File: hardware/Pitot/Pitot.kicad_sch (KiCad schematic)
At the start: 35 parts, among them J1 53307-2471, J3 MX150_02x06_Vertical, J4 Conn_01x07, U2 LDO40LPURY

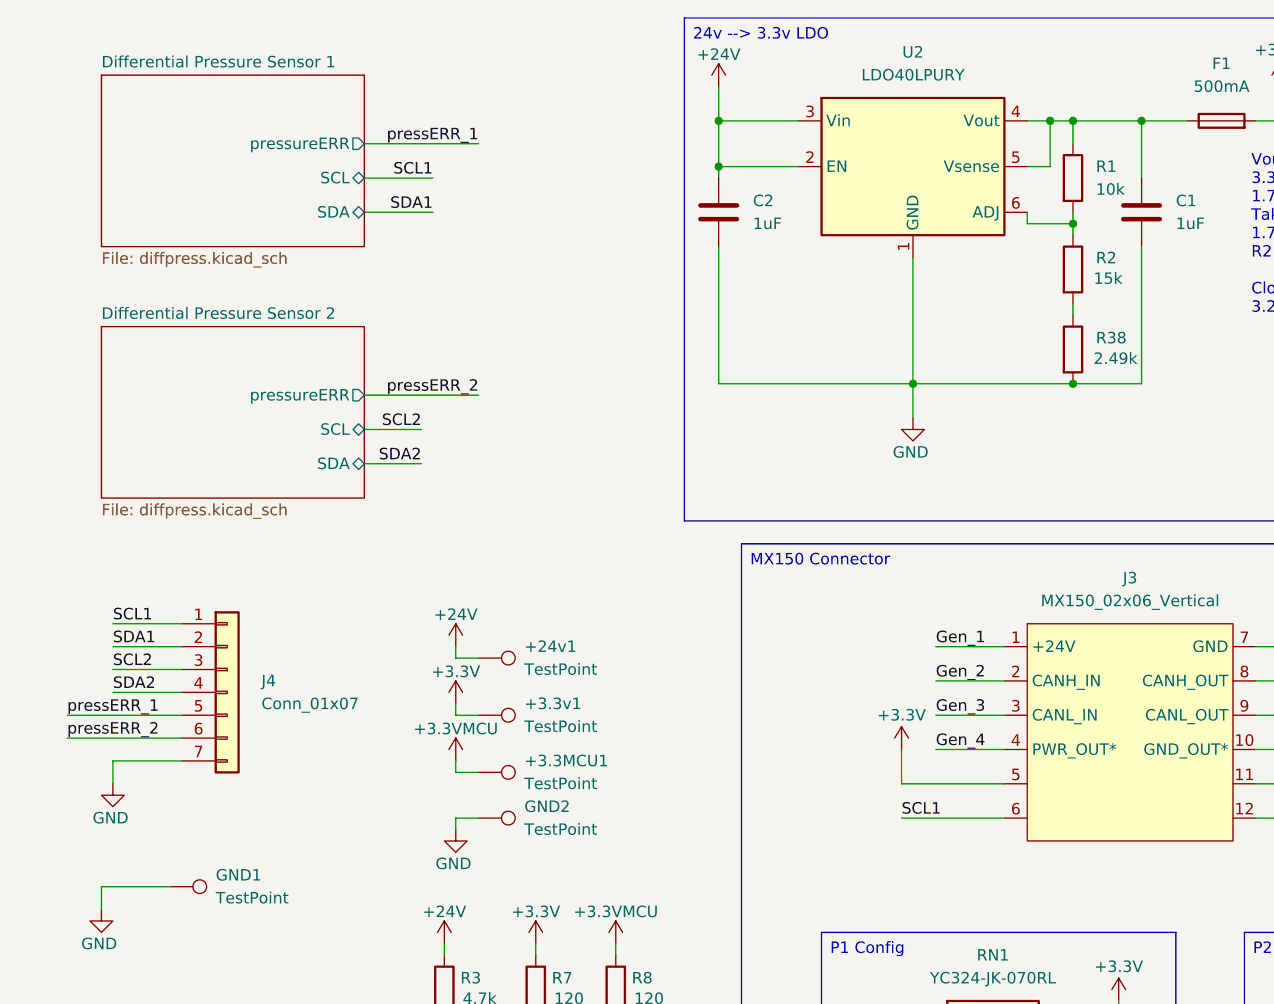
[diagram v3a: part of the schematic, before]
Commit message: final pitot board + bom files
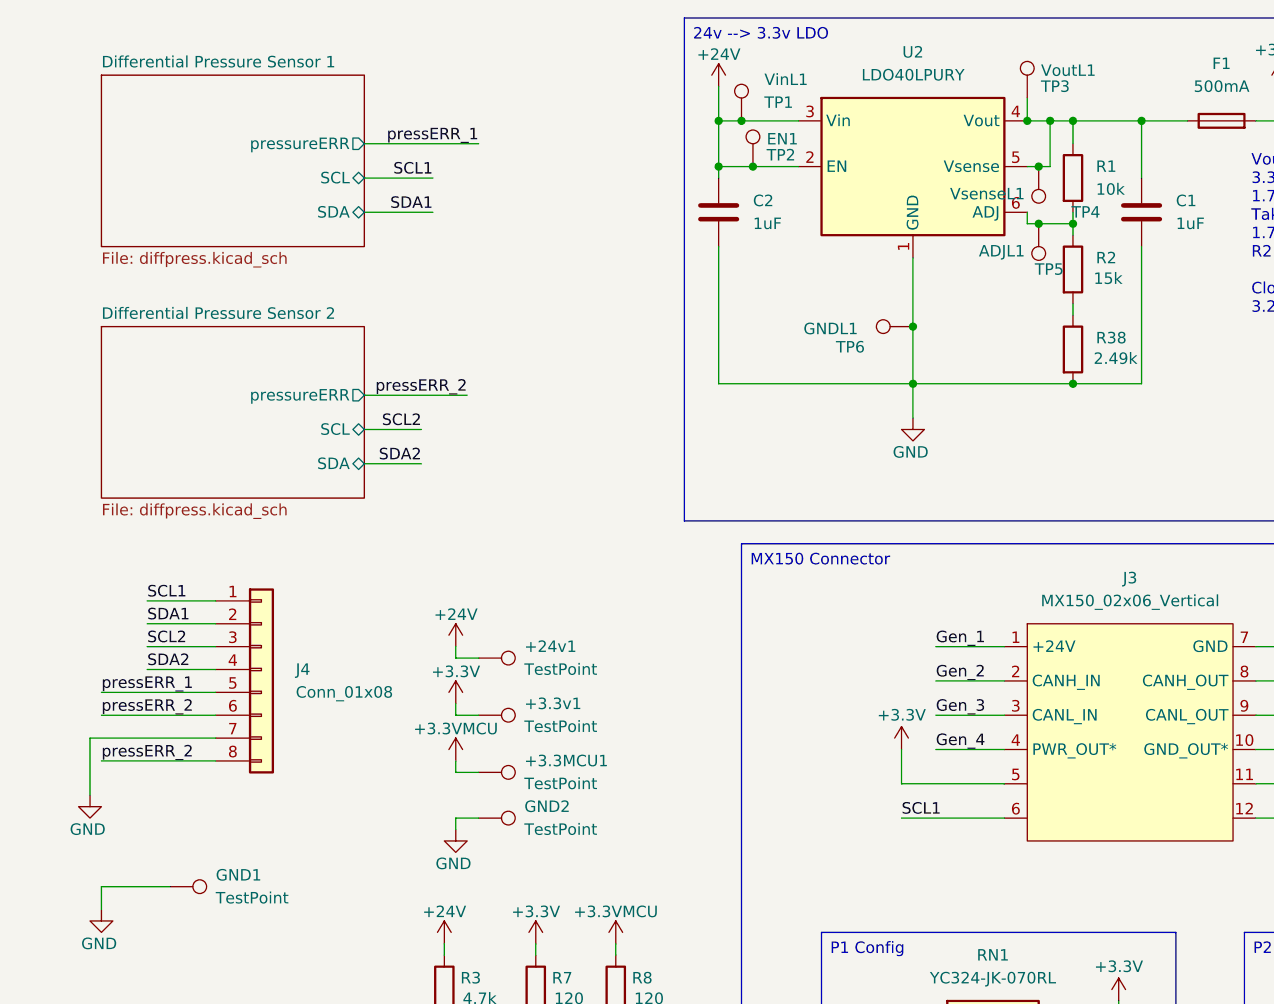
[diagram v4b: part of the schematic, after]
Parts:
- removed J4: Conn_01x07, Connector_PinHeader_2.54mm:PinHeader_2x04_P2.54mm_Vertical, symbol Connector_Generic:Conn_01x07
- added ADJL1: TP5, TestPoint:TestPoint_Pad_D1.0mm, symbol Connector:TestPoint
- added EN1: TP2, TestPoint:TestPoint_Pad_D1.0mm, symbol Connector:TestPoint
- added GNDL1: TP6, TestPoint:TestPoint_Pad_D1.0mm, symbol Connector:TestPoint
- added J4: Conn_01x08, Connector_PinHeader_2.54mm:PinHeader_2x04_P2.54mm_Vertical, symbol Connector_Generic:Conn_01x08
- added VinL1: TP1, TestPoint:TestPoint_Pad_D1.0mm, symbol Connector:TestPoint
- added VoutL1: TP3, TestPoint:TestPoint_Pad_D1.0mm, symbol Connector:TestPoint
- added VsenseL1: TP4, TestPoint:TestPoint_Pad_D1.0mm, symbol Connector:TestPoint
- D3: P/N NCD0603R1 -> XL-1608UBC-06A
- F1: P/N 534-3568 -> 3568
- R3: P/N CRCW06031K00FKEI -> CRCW06034K70FKEA
- RN1, RN2: P/N 603-YC324-JK-070RL -> YC324-JK-070RL
- U2: P/N 511-LDO40LPU33RY -> LDO40LPU33RY
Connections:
- net +24V: now also EN1.1, VinL1.1
- net GND: now also GNDL1.1, J4.7 (Pin_7)
- net SCL1: now also J4.1 (Pin_1)
- net SCL2: now also J4.3 (Pin_3)
- net SDA1: now also J4.2 (Pin_2)
- net SDA2: now also J4.4 (Pin_4)
- net pressERR_1: now also J4.5 (Pin_5)
- net pressERR_2: now also J4.6 (Pin_6), J4.8 (Pin_8)
- net at R1.2, R2.1, U2.6 (ADJ): now also ADJL1.1
- net at C1.1, F1.1, R1.1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: now also VoutL1.1, VsenseL1.1

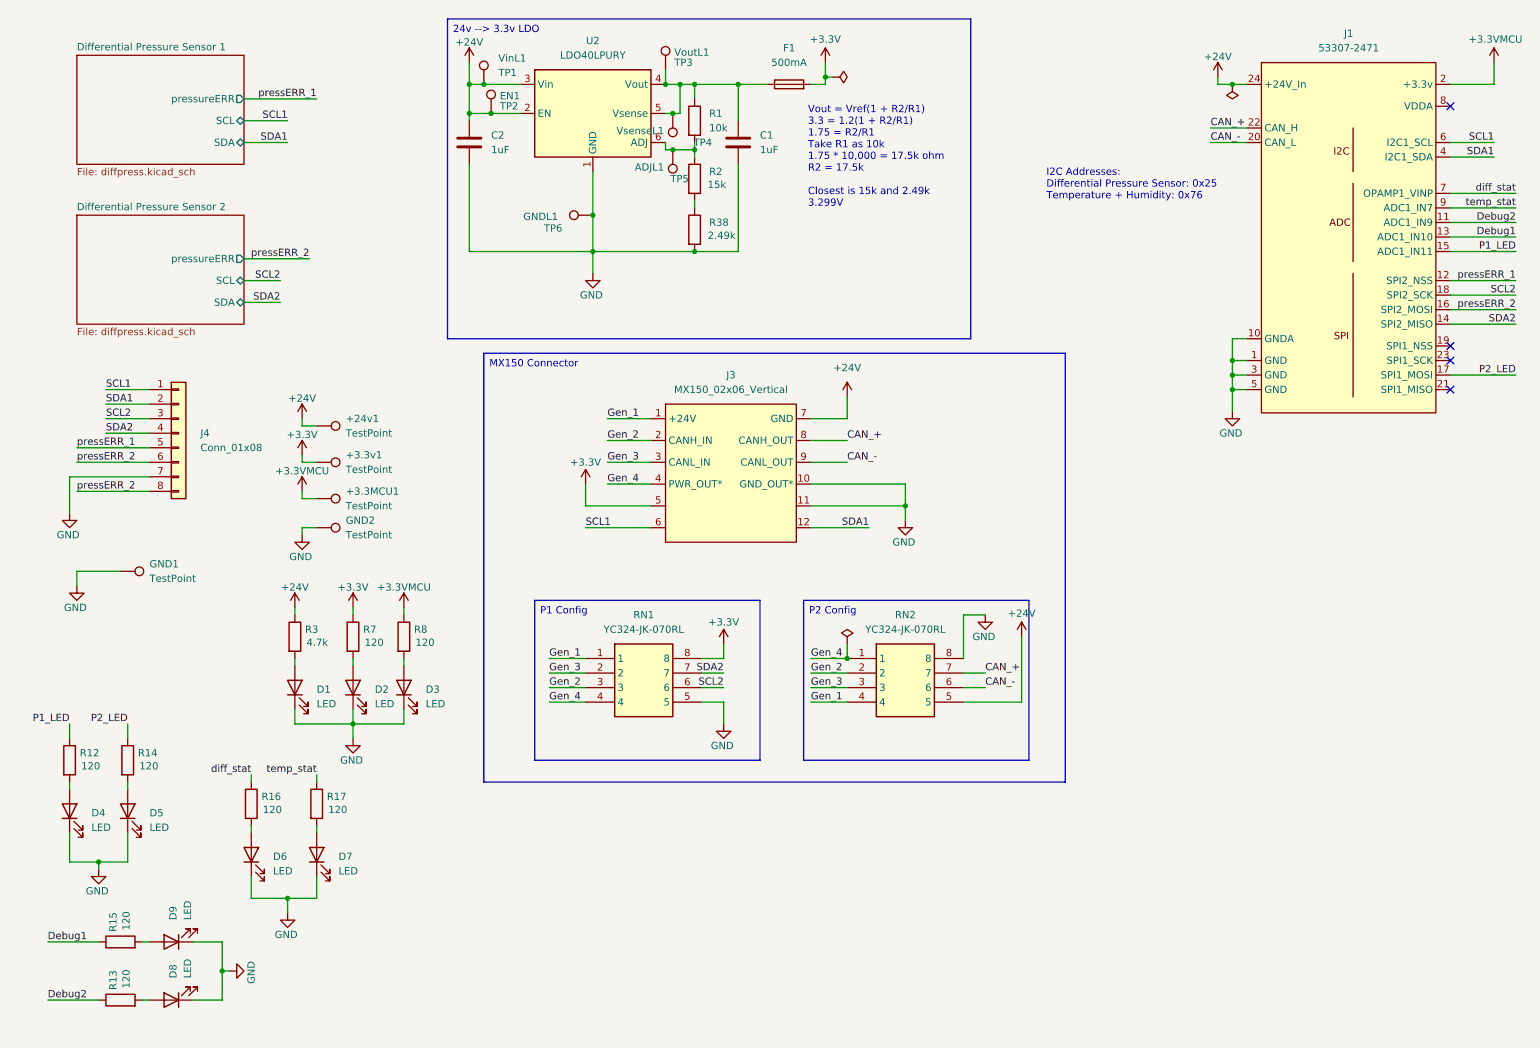
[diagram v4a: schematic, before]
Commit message: Rev B Review (#2)
* schematic changes: ldo switched out of qfn, op amp footprint fixed, resistor array changed. need add correct stm changes

* finished sch + removed LDO

* removed LDO, added correct cube.

* op-amp changes

* layout finished, need to add some more silkscreen + ready for review!

* finished layout + silkscreen, ready to review.

* mac files removed

* made changes from review council

* added 3d models for 01x05 nanofits

* added stepfiles for sus-rh

* sus-rh production ready

* remove .DS_Store files

* fixed nanofit for linpot

* added "validated silkscreen"

* Added jlc assembly files

* pitot board sch review. the biggest change was the switch to nanofits and different pressure sensor

---------

Co-authored-by: Lakshay983 <56173382+Lakshay983@users.noreply.github.com>
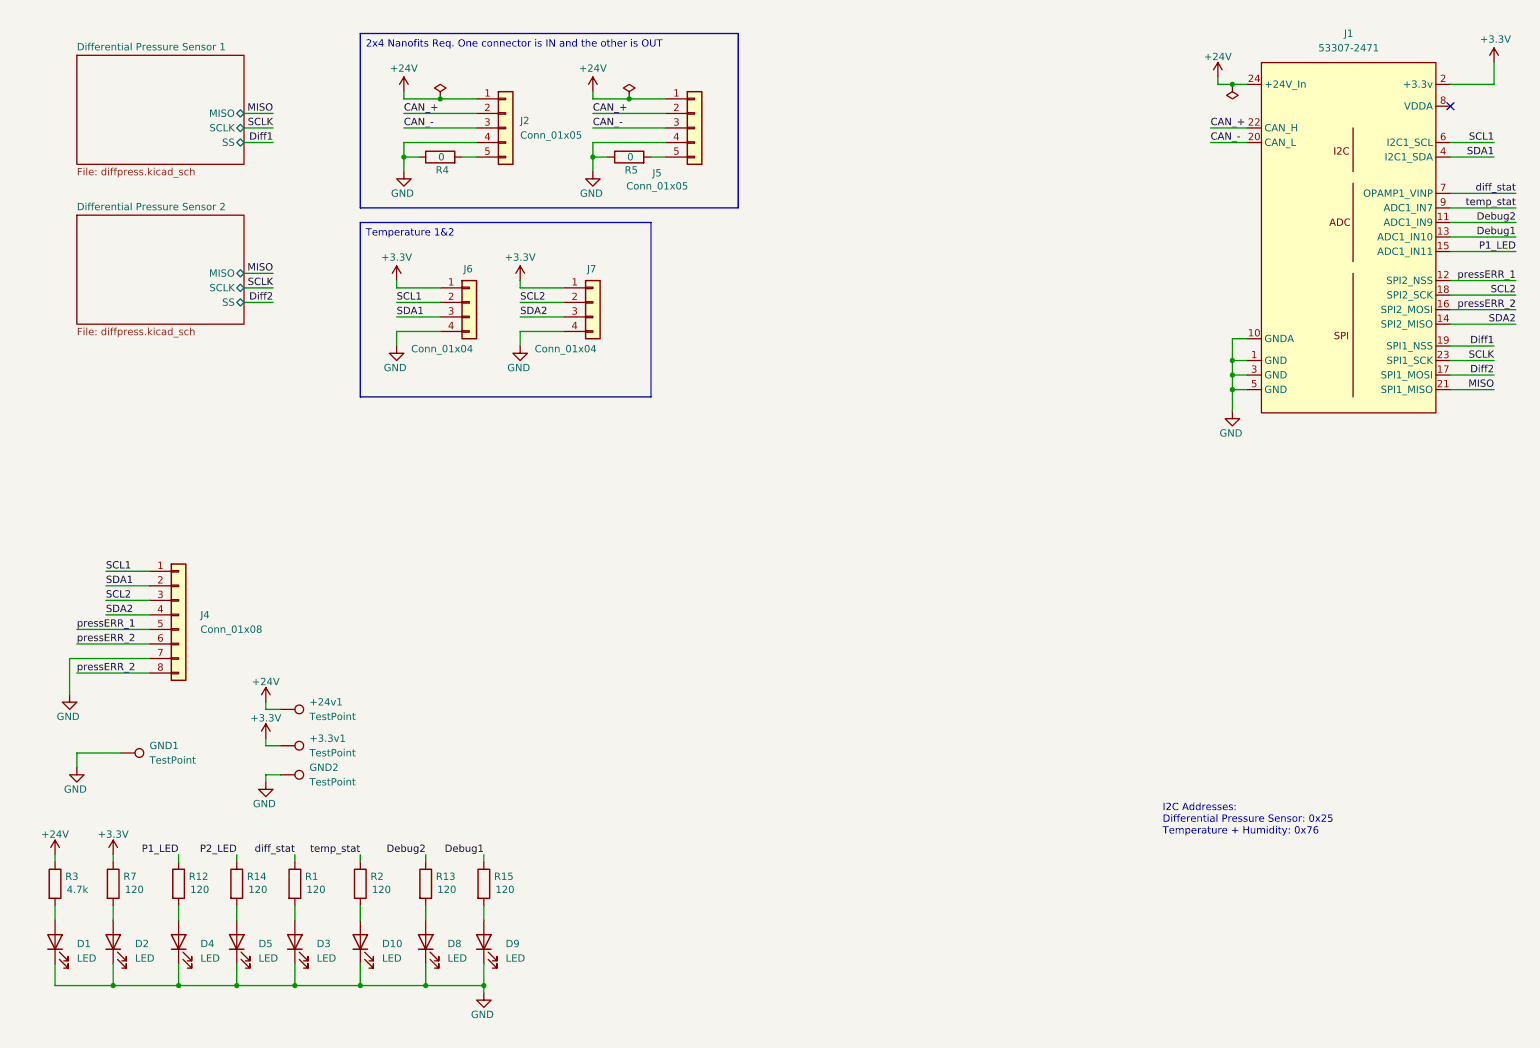
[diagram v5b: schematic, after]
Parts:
- removed +3.3MCU1: TestPoint, TestPoint:TestPoint_Pad_1.0x1.0mm, symbol Connector:TestPoint
- removed ADJL1: TP5, TestPoint:TestPoint_Pad_D1.0mm, symbol Connector:TestPoint
- removed C1, C2: 1uF, Capacitor_SMD:C_0603_1608Metric_Pad1.08x0.95mm_HandSolder, symbol Device:C
- removed D6, D7: LED, LED_SMD:LED_0603_1608Metric_Pad1.05x0.95mm_HandSolder, symbol Device:LED
- removed EN1: TP2, TestPoint:TestPoint_Pad_D1.0mm, symbol Connector:TestPoint
- removed F1: 500mA, Fuse:Fuseholder_Blade_Mini_Keystone_3568, symbol Device:Fuse
- removed GNDL1: TP6, TestPoint:TestPoint_Pad_D1.0mm, symbol Connector:TestPoint
- removed J3: MX150_02x06_Vertical, UTSVT_Connectors:MX150_02x06_Vertical, symbol utsvt_connectors:MX150_02x06_Vertical
- removed R16, R17, R8: 120, Resistor_SMD:R_0603_1608Metric_Pad0.98x0.95mm_HandSolder, symbol Device:R
- removed R38: 2.49k, Resistor_SMD:R_0603_1608Metric_Pad0.98x0.95mm_HandSolder, symbol Device:R
- removed RN1, RN2: YC324-JK-070RL, 4pinRes:YC324JK07220RL, symbol resistorArray:YC324-JK-070RL
- removed U2: LDO40LPURY, Package_DFN_QFN:DFN-6-1EP_3x3mm_P0.95mm_EP1.7x2.6mm, symbol Regulator_Linear:LDO40LPURY
- removed VinL1: TP1, TestPoint:TestPoint_Pad_D1.0mm, symbol Connector:TestPoint
- removed VoutL1: TP3, TestPoint:TestPoint_Pad_D1.0mm, symbol Connector:TestPoint
- removed VsenseL1: TP4, TestPoint:TestPoint_Pad_D1.0mm, symbol Connector:TestPoint
- added D10: LED, LED_SMD:LED_0603_1608Metric_Pad1.05x0.95mm_HandSolder, symbol Device:LED
- added J2, J5: Conn_01x05, symbol Connector_Generic:Conn_01x05
- added J6, J7: Conn_01x04, symbol Connector_Generic:Conn_01x04
- added R4, R5: 0, Resistor_SMD:R_0603_1608Metric_Pad0.98x0.95mm_HandSolder, symbol Device:R
- D1, D5, D8: JLC P/N (none) -> C7371904; P/N NCD0603R1 -> XL-1608UBC-06A
- D2, D4, D9: JLC P/N (none) -> C84263
- D3: JLC P/N (none) -> C84263; P/N XL-1608UBC-06A -> NCD0603R1
- R1: value 10k -> 120; P/N CRCW060310K0FKEI -> CRCW06031K00FKEI
- R2: value 15k -> 120; P/N CRCW060315K0FKEA -> CRCW06031K00FKEI
- R3: P/N CRCW06034K70FKEA -> XL-1608UBC-06A
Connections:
- net +3.3VMCU is gone; now on net +3.3V: J1.2 (+3.3v)
- net +24V: now also J2.1 (Pin_1), J5.1 (Pin_1)
- net +3.3V: now also J6.1 (Pin_1), J7.1 (Pin_1)
- net CAN_+: now also J2.2 (Pin_2), J5.2 (Pin_2)
- net CAN_-: now also J2.3 (Pin_3), J5.3 (Pin_3)
- net GND: now also D10.1 (K), J2.4 (Pin_4), J5.4 (Pin_4), J6.4 (Pin_4), J7.4 (Pin_4), R4.1, R5.1
- net P2_LED: no longer J1.17 (SPI1_MOSI)
- net SCL1: now also J6.2 (Pin_2)
- net SCL2: now also J7.2 (Pin_2)
- net SDA1: now also J6.3 (Pin_3)
- net SDA2: now also J7.3 (Pin_3)
- net diff_stat: now also R1.1
- net temp_stat: now also R2.1
- net at R1.2: now also D3.2 (A); no longer R2.1
- net at R2.2: now also D10.2 (A)
- net Diff1: now reaches J1.19 (SPI1_NSS)
- net MISO: now reaches J1.21 (SPI1_MISO)
- net SCLK: now reaches J1.23 (SPI1_SCK)
- new net: J5.5 (Pin_5), R5.2
- new net: J2.5 (Pin_5), R4.2
- new net Diff2: J1.17 (SPI1_MOSI)
- no-connect marks 4 -> 1
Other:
- sheet Differential Pressure Sensor 1 ports: added MISO, SCLK, SS; removed SCL, SDA, pressureERR
- sheet Differential Pressure Sensor 2 ports: added MISO, SCLK, SS; removed SCL, SDA, pressureERR
- note removed: "Vout = Vref(1 + R2/R1) 3.3 = 1.2(1 + R2/R1) 1.75 = R2/R1 Take R1 as 10k 1.75 * 10,000 = 17.5k ohm R2 = 17.5k Closest is 15k and 2.49k 3.299V"
- moved on the sheet: +24v1, +3.3v1, D1, D4, D5, D8, D9, GND1, GND2, J4, R12, R13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
